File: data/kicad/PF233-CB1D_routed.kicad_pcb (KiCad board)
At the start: 6 copper layers, 78 x 77.2 mm, 70 parts, among them M5 5 V 1.5 A switching module, U1 Pico 2 W

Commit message: WIP: per-board 0.125 mm routing grid for AU1 / CB1D (0.5 mm-pitch rows on grid lines); fine zone radius in mm; AU1 route on the new grid running
Co-Authored-By: Claude Opus 5.5 <noreply@anthropic.com>
Claude-Session: https://claude.ai/code/session_01FX4DWSYYjMCFGGA6gmha65
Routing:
- net GYR_SDA: track 11.2 -> 6.59 mm, vias 2 -> 1
- net UG_VIO: track 14.9 -> 18.9 mm
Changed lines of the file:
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@@
   (gr_line (start 107.600 136.500) (end 92.400 136.500) (stroke (width 0.1) (type default)) (layer "Edge.Cuts"))
   (gr_line (start 92.400 136.500) (end 92.400 138.252) (stroke (width 0.1) (type default)) (layer "Edge.Cuts"))
-  (segment (start 106.9500 68.7000) (end 106.9500 69.3000) (width 0.2) (layer "F.Cu") (net 15))
-  (segment (start 106.9500 69.3000) (end 107.0000 68.5875) (width 0.2) (layer "F.Cu") (net 15))
-  (segment (start 106.5000 68.4000) (end 106.5000 67.9500) (width 0.2) (layer "F.Cu") (net 15))
-  (segment (start 106.5000 67.9500) (end 106.3500 67.8000) (width 0.2) (layer "F.Cu") (net 15))
-  (segment (start 106.3500 67.8000) (end 105.7750 67.0000) (width 0.2) (layer "F.Cu") (net 15))
+  (segment (start 106.9500 68.7000) (end 106.9500 69.3000) (width 0.15) (layer "F.Cu") (net 15))
+  (segment (start 106.9500 69.3000) (end 107.0000 68.5875) (width 0.15) (layer "F.Cu") (net 15))
+  (segment (start 106.5000 68.4000) (end 106.5000 67.9500) (width 0.15) (layer "F.Cu") (net 15))
+  (segment (start 106.5000 67.9500) (end 106.3500 67.8000) (width 0.15) (layer "F.Cu") (net 15))
+  (segment (start 106.3500 67.8000) (end 105.7750 67.0000) (width 0.15) (layer "F.Cu") (net 15))
   (segment (start 108.8900 75.1100) (end 108.4500 74.4000) (width 0.2) (layer "F.Cu") (net 16))
   (segment (start 108.4500 74.4000) (end 108.4500 72.3000) (width 0.2) (layer "F.Cu") (net 16))
-  (segment (start 108.4500 72.3000) (end 106.9500 70.8000) (width 0.2) (layer "F.Cu") (net 16))
-  (segment (start 106.9500 70.8000) (end 106.9500 70.5000) (width 0.2) (layer "F.Cu") (net 16))
+  (segment (start 108.4500 72.3000) (end 107.1000 70.9500) (width 0.15) (layer "F.Cu") (net 16))
+  (segment (start 107.1000 70.9500) (end 107.1000 70.6500) (width 0.15) (layer "F.Cu") (net 16))
+  (segment (start 107.1000 70.6500) (end 106.9500 70.5000) (width 0.15) (layer "F.Cu") (net 16))
   (segment (start 108.4500 72.3000) (end 109.5000 72.3000) (width 0.2) (layer "F.Cu") (net 16))
   (segment (start 109.5000 72.3000) (end 110.4000 71.4000) (width 0.2) (layer "F.Cu") (net 16))
@@
   (segment (start 112.3250 69.5000) (end 111.9000 70.0500) (width 0.2) (layer "F.Cu") (net 17))
   (segment (start 111.9000 70.0500) (end 112.3250 69.5000) (width 0.2) (layer "F.Cu") (net 17))
-  (segment (start 111.9000 70.8000) (end 108.7500 70.8000) (width 0.2) (layer "In2.Cu") (net 17))
-  (segment (start 108.7500 70.8000) (end 107.7000 70.8000) (width 0.2) (layer "F.Cu") (net 17))
-  (segment (start 107.7000 70.8000) (end 107.5500 70.6500) (width 0.2) (layer "F.Cu") (net 17))
-  (segment (start 107.5500 70.6500) (end 107.5500 70.5000) (width 0.2) (layer "F.Cu") (net 17))
-  (segment (start 108.0000 70.2000) (end 108.0000 69.7500) (width 0.2) (layer "F.Cu") (net 50))
-  (segment (start 108.0000 69.7500) (end 108.0000 69.3000) (width 0.2) (layer "F.Cu") (net 50))
-  (segment (start 108.0000 69.3000) (end 107.7000 69.3000) (width 0.2) (layer "F.Cu") (net 50))
-  (segment (start 107.7000 69.3000) (end 107.7000 69.1500) (width 0.2) (layer "F.Cu") (net 50))
-  (segment (start 107.7000 69.1500) (end 107.5500 69.1500) (width 0.2) (layer "F.Cu") (net 50))
-  (segment (start 107.5500 69.1500) (end 107.5500 68.7000) (width 0.2) (layer "F.Cu") (net 50))
-  (segment (start 107.5500 68.7000) (end 107.5500 67.6500) (width 0.2) (layer "F.Cu") (net 50))
-  (segment (start 107.5500 67.6500) (end 107.2250 67.0000) (width 0.2) (layer "F.Cu") (net 50))
-  (segment (start 107.2250 67.0000) (end 107.5500 67.6500) (width 0.2) (layer "F.Cu") (net 50))
-  (segment (start 107.5500 67.6500) (end 107.5500 66.9000) (width 0.2) (layer "F.Cu") (net 50))
-  (segment (start 107.5500 66.9000) (end 106.6500 66.0000) (width 0.2) (layer "F.Cu") (net 50))
+  (segment (start 108.0000 70.2000) (end 108.0000 69.7500) (width 0.15) (layer "F.Cu") (net 50))
+  (segment (start 108.0000 69.7500) (end 108.0000 69.3000) (width 0.15) (layer "F.Cu") (net 50))
+  (segment (start 108.0000 69.3000) (end 107.8500 69.3000) (width 0.15) (layer "F.Cu") (net 50))
+  (segment (start 107.8500 69.3000) (end 107.7000 69.1500) (width 0.15) (layer "F.Cu") (net 50))
+  (segment (start 107.7000 69.1500) (end 107.5500 69.1500) (width 0.15) (layer "F.Cu") (net 50))
+  (segment (start 107.5500 69.1500) (end 107.5500 68.7000) (width 0.15) (layer "F.Cu") (net 50))
+  (segment (start 107.5500 68.7000) (end 107.5500 67.6500) (width 0.15) (layer "F.Cu") (net 50))
+  (segment (start 107.5500 67.6500) (end 107.2250 67.0000) (width 0.15) (layer "F.Cu") (net 50))
+  (segment (start 107.2250 67.0000) (end 107.5500 67.6500) (width 0.15) (layer "F.Cu") (net 50))
+  (segment (start 107.5500 67.6500) (end 107.5500 66.9000) (width 0.15) (layer "F.Cu") (net 50))
+  (segment (start 107.5500 66.9000) (end 106.6500 66.0000) (width 0.15) (layer "F.Cu") (net 50))
   (segment (start 106.6500 66.0000) (end 106.5000 66.0000) (width 0.2) (layer "F.Cu") (net 50))
   (segment (start 106.5000 66.0000) (end 106.3500 65.8500) (width 0.2) (layer "F.Cu") (net 50))
@@
   (segment (start 104.7000 66.4500) (end 104.2250 67.0000) (width 0.2) (layer "F.Cu") (net 50))
   (segment (start 104.2250 67.0000) (end 104.7000 66.4500) (width 0.2) (layer "F.Cu") (net 50))
-  (segment (start 104.7000 66.4500) (end 104.7000 68.4000) (width 0.2) (layer "F.Cu") (net 50))
-  (segment (start 104.7000 68.4000) (end 104.2500 68.8500) (width 0.2) (layer "F.Cu") (net 50))
-  (segment (start 104.2500 68.8500) (end 103.8250 69.5000) (width 0.2) (layer "F.Cu") (net 50))
-  (segment (start 104.7000 68.4000) (end 105.4500 68.4000) (width 0.2) (layer "F.Cu") (net 50))
-  (segment (start 105.4500 68.4000) (end 105.7500 68.7000) (width 0.2) (layer "F.Cu") (net 50))
+  (segment (start 104.7000 66.4500) (end 104.7000 68.4000) (width 0.15) (layer "F.Cu") (net 50))
+  (segment (start 104.7000 68.4000) (end 104.2500 68.8500) (width 0.15) (layer "F.Cu") (net 50))
+  (segment (start 104.2500 68.8500) (end 103.8250 69.5000) (width 0.15) (layer "F.Cu") (net 50))
+  (segment (start 104.7000 68.4000) (end 105.4500 68.4000) (width 0.15) (layer "F.Cu") (net 50))
+  (segment (start 105.4500 68.4000) (end 105.7500 68.7000) (width 0.15) (layer "F.Cu") (net 50))
+  (segment (start 105.8375 68.7500) (end 105.6000 68.5500) (width 0.15) (layer "F.Cu") (net 50))
+  (segment (start 105.6000 68.5500) (end 105.3000 68.8500) (width 0.15) (layer "F.Cu") (net 50))
+  (segment (start 105.3000 68.8500) (end 105.3000 70.6500) (width 0.15) (layer "F.Cu") (net 50))
+  (segment (start 105.3000 70.6500) (end 106.3500 70.6500) (width 0.15) (layer "F.Cu") (net 50))
+  (segment (start 106.3500 70.6500) (end 106.3500 70.3500) (width 0.15) (layer "F.Cu") (net 50))
+  (segment (start 106.3500 70.3500) (end 106.5000 70.3500) (width 0.15) (layer "F.Cu") (net 50))
   (segment (start 88.9500 98.0000) (end 88.3500 98.7000) (width 0.2) (layer "F.Cu") (net 15))
   (segment (start 88.3500 98.7000) (end 88.3500 99.1500) (width 0.2) (layer "F.Cu") (net 15))
@@
   (segment (start 108.3000 66.4500) (end 108.3000 66.0000) (width 0.2) (layer "F.Cu") (net 15))
   (segment (start 108.3000 66.0000) (end 108.7750 67.0000) (width 0.2) (layer "F.Cu") (net 15))
-  (segment (start 105.7750 67.0000) (end 106.2000 67.6500) (width 0.2) (layer "F.Cu") (net 15))
-  (segment (start 106.2000 67.6500) (end 106.2000 68.1000) (width 0.2) (layer "F.Cu") (net 15))
-  (segment (start 106.2000 68.1000) (end 106.5000 68.5875) (width 0.2) (layer "F.Cu") (net 15))
+  (segment (start 105.7750 67.0000) (end 106.2000 67.6500) (width 0.15) (layer "F.Cu") (net 15))
+  (segment (start 106.2000 67.6500) (end 106.2000 68.1000) (width 0.15) (layer "F.Cu") (net 15))
+  (segment (start 106.2000 68.1000) (end 106.5000 68.5875) (width 0.15) (layer "F.Cu") (net 15))
   (segment (start 99.7000 95.5550) (end 98.8500 95.2500) (width 0.3) (layer "F.Cu") (net 31))
   (segment (start 98.8500 95.2500) (end 98.4000 95.2500) (width 0.3) (layer "F.Cu") (net 31))
@@
   (segment (start 126.6000 77.4000) (end 126.7250 78.0000) (width 0.2) (layer "F.Cu") (net 51))
   (segment (start 98.4000 120.9000) (end 98.8500 120.7500) (width 0.2) (layer "F.Cu") (net 15))
-  (segment (start 106.2000 68.1000) (end 106.3500 67.8000) (width 0.2) (layer "F.Cu") (net 15))
+  (segment (start 106.2000 68.1000) (end 106.3500 67.8000) (width 0.15) (layer "F.Cu") (net 15))
   (segment (start 111.0000 73.0500) (end 110.8500 73.0500) (width 0.2) (layer "F.Cu") (net 11))
   (segment (start 111.0000 73.0500) (end 110.8500 73.0500) (width 0.2) (layer "In3.Cu") (net 11))
@@
   (via (at 106.3500 67.8000) (size 0.6) (drill 0.3) (layers "F.Cu" "B.Cu") (net 15))
   (via (at 111.9000 70.0500) (size 0.6) (drill 0.3) (layers "F.Cu" "B.Cu") (net 17))
-  (via (at 108.7500 70.8000) (size 0.6) (drill 0.3) (layers "F.Cu" "B.Cu") (net 17))
   (via (at 88.3500 99.1500) (size 0.6) (drill 0.3) (layers "F.Cu" "B.Cu") (net 15))
   (via (at 86.8500 94.5000) (size 0.6) (drill 0.3) (layers "F.Cu" "B.Cu") (net 15))

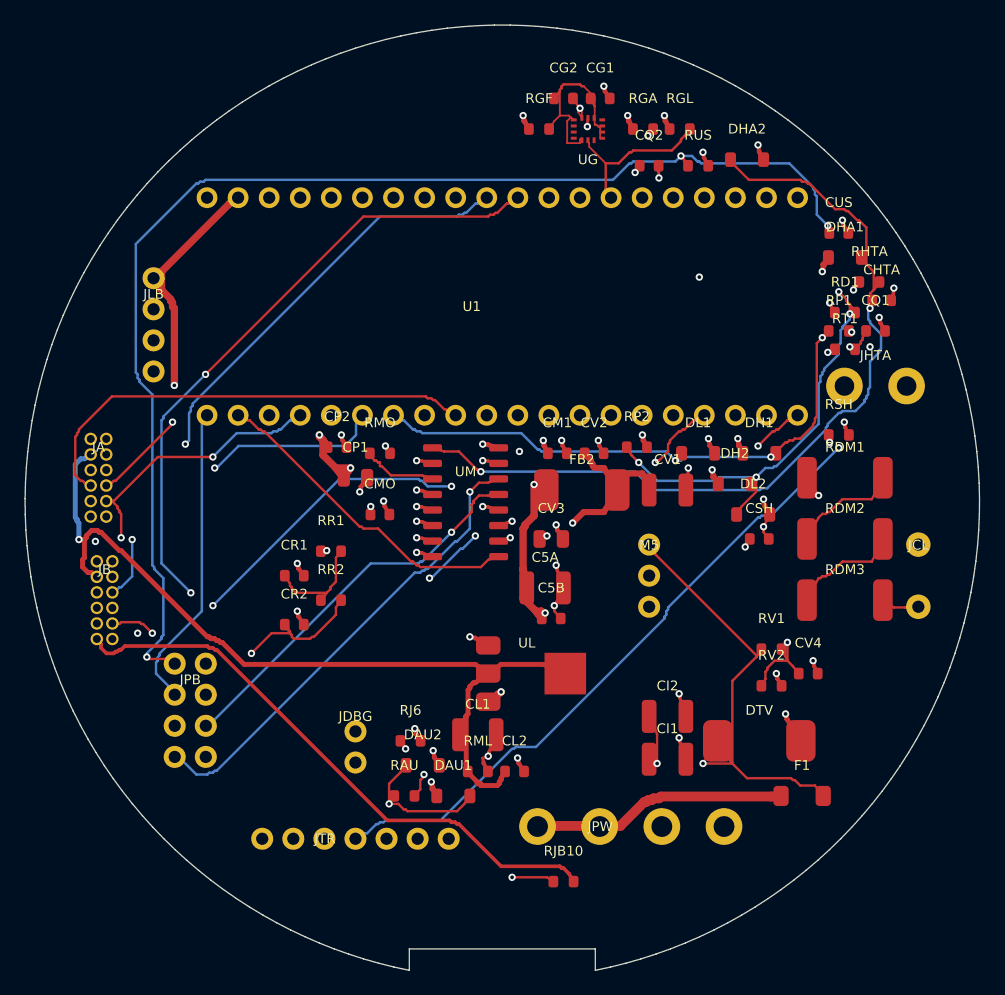
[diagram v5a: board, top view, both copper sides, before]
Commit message: WIP (NOT signed off): sign-off outputs with AU1 38 / 38 (exact DRC 0 / 0, all AU1 checks pass); CB1D 45 / 46 (TRIG_EXT open on the 0.125 grid, being re-routed on 0.15)
Co-Authored-By: Claude Opus 5.5 <noreply@anthropic.com>
Claude-Session: https://claude.ai/code/session_01FX4DWSYYjMCFGGA6gmha65
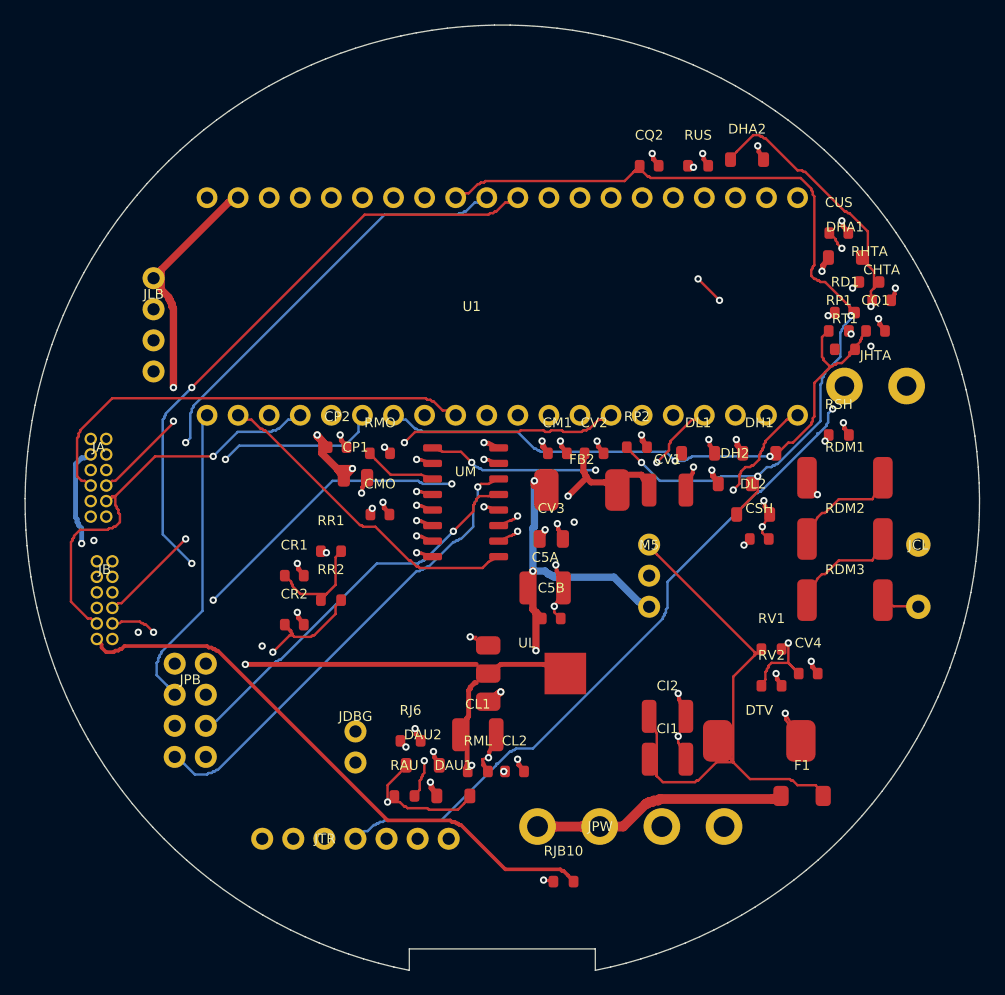
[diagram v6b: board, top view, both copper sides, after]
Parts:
- removed CG1, CG2: 100n, Capacitor_SMD:C_0603_1608Metric
- removed RGA, RGL: 4k7, Resistor_SMD:R_0603_1608Metric
- removed RGF: 10R, Resistor_SMD:R_0603_1608Metric
- removed UG: BMI270, PF233:BMI270_LGA-14_2.5x3.0mm
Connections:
- U1 pad 26: GYR_SDA -> (no net)
- U1 pad 27: GYR_SCL -> (no net)
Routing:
- net TRIG_EXT: track 64.4 -> 0.00 mm, vias 1 -> 0
- net UG_VIO: track 18.9 -> 0.00 mm
- net GYR_SCL: track 13.5 -> 0.00 mm
- net GND: track 117.3 -> 109.0 mm, vias 42 -> 39
- net P3V3: track 26.7 -> 19.4 mm, vias 12 -> 9
- net GYR_SDA: track 6.59 -> 0.00 mm, vias 1 -> 0
- net DIAL_EXT: track 71.0 -> 65.2 mm
- net UMB_SHLD: track 103.9 -> 99.8 mm
- net BLANK: track 38.0 -> 34.3 mm, vias 2 -> 1
- net +5V: track 96.5 -> 98.7 mm, vias 6 -> 7
- net AUD_PIO: track 46.1 -> 47.6 mm
- net MUX_S0: track 52.7 -> 51.2 mm
- net MUX_S1: track 54.1 -> 52.7 mm
- net +3V3D: track 75.0 -> 73.7 mm, vias 1 -> 4
- net JB10_VCM: track 44.8 -> 46.0 mm
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
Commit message: WIP: sign-off outputs (73 PASS / 1 FAIL before the HV count fix; rerun in progress)
Co-Authored-By: Claude Opus 5.5 <noreply@anthropic.com>
Claude-Session: https://claude.ai/code/session_01FX4DWSYYjMCFGGA6gmha65
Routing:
- net TRIG_EXT: track 0.00 -> 64.4 mm, vias 0 -> 1
- net DIAL_EXT: track 65.2 -> 71.0 mm
- net BLANK: track 34.3 -> 38.0 mm, vias 1 -> 2
- net UMB_SHLD: track 99.8 -> 102.1 mm
- net +5V: track 98.7 -> 96.5 mm, vias 7 -> 6
- net HTA_IN: track 72.6 -> 74.3 mm, vias 3 -> 2
- net AUD_PIO: track 47.6 -> 46.1 mm
- net MUX_S0: track 51.2 -> 52.7 mm
- net DIAL_IN: track 80.4 -> 78.9 mm
- net GND: track 109.0 -> 110.3 mm
- net MUX_S1: track 52.7 -> 54.1 mm
- net +3V3D: track 73.7 -> 75.0 mm, vias 4 -> 1
- net JB10_VCM: track 46.0 -> 44.8 mm
- net VBUS_SENSE: track 73.4 -> 72.7 mm, vias 3 -> 2
- net SCLK: track 38.1 -> 38.8 mm
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
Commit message: Close-out of the output modes / audio / gyro integration: sign-off 76 PASS / 0 FAIL / 4 UNVERIFIED, strict regress 114 / 0, release controls 12 / 12, publish 0 stale
AU1 (36 x 60, 8 layers, gyro moved from CB1D) routed 38 / 38, CB1D-C2 46 / 46, both exact DRC 0 / 0; PB1R-v5 AWG12 solder holes; PM2-B, HB2-B; superseded Gerber sets marked.
Tooling now default: exact-geometry DRC, router fine-pitch keep-out / neck-down / per-board grid, local repair, round checkpoints, non-destructive reset,
interface check, AU1 3-D models with gull-wing leads, counted HV check; pad check traced by the pipeline; process-guard regress row; PROCESS.md / CLAUDE.md / handoff updated.

Co-Authored-By: Claude Opus 5.5 <noreply@anthropic.com>
Claude-Session: https://claude.ai/code/session_01FX4DWSYYjMCFGGA6gmha65
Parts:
- removed the JCL at (134.0, 106.0)
- removed the JDBG at (88.0, 120.0)
- removed the JPB at (74.5, 117.0)
- removed the JPW at (110.5, 126.5)
- removed the JTR at (88.0, 127.5)
- added JCL: Coil taps from TXJ1: COIL_B (drain side), COIL_A (VBUS side), Connector:Wire_pads_AWG22_1x2_P5.08mm, F.Cu at (134.0, 106.0)
- added JDBG: RUN / GND (reset, SWD pads on Pico underside), Connector:Wire_pads_1x2_P2.54mm, F.Cu at (88.0, 120.0)
- added JPB: to PB1R: 12V GND TX1_IN REF_I1 FAULT1_N ISENSE1 NTC GND, Connector:Wire_pads_2x4_P2.54mm, F.Cu at (74.5, 117.0)
- added JPW: Power in: VBUS VBUS GND GND (from shaft), Connector:Wire_pads_1x4_P5.08mm, F.Cu at (110.5, 126.5)
- added JTR: Handle: +3V3 GND TRIG DIAL AUD_LINK - SHLD, Connector:Wire_pads_1x7_P2.54mm, F.Cu at (88.0, 127.5)
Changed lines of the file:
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@@
     (pad "40" thru_hole circle (at 8.890 -24.130 90) (size 1.7 1.7) (drill 1.0) (layers "*.Cu" "*.Mask") (net 0 ""))
   )
-  (footprint "Connector:Pin_header_1x2_P2.54mm" (layer "F.Cu") (at 88.0000 120.0000)
+  (footprint "Connector:Wire_pads_1x2_P2.54mm" (layer "F.Cu") (at 88.0000 120.0000)
     (property "Reference" "JDBG" (at 0 -2.5 0) (layer "F.SilkS") (effects (font (size 0.8 0.8) (thickness 0.12))))
     (property "Value" "RUN / GND (reset, SWD pads on Pico underside)" (at 0 2.5 0) (layer "F.Fab") (effects (font (size 0.8 0.8) (thickness 0.12))))
@@
     (pad "2" smd roundrect (at 0.775 0.000) (size 0.800 0.950) (layers "F.Cu" "F.Paste" "F.Mask") (net 15 "GND"))
   )
-  (footprint "Connector:Terminal_block_1x4_P5.08mm" (layer "F.Cu") (at 110.5000 126.5000 90)
+  (footprint "Connector:Wire_pads_1x4_P5.08mm" (layer "F.Cu") (at 110.5000 126.5000 90)
     (property "Reference" "JPW" (at 0 -2.5 0) (layer "F.SilkS") (effects (font (size 0.8 0.8) (thickness 0.12))))
     (property "Value" "Power in: VBUS VBUS GND GND (from shaft)" (at 0 2.5 0) (layer "F.Fab") (effects (font (size 0.8 0.8) (thickness 0.12))))
@@
     (pad "2" smd roundrect (at 0.775 0.000) (size 0.800 0.950) (layers "F.Cu" "F.Paste" "F.Mask") (net 15 "GND"))
   )
-  (footprint "Connector:Pin_header_1x7_P2.54mm" (layer "F.Cu") (at 88.0000 127.5000 90)
+  (footprint "Connector:Wire_pads_1x7_P2.54mm" (layer "F.Cu") (at 88.0000 127.5000 90)
     (property "Reference" "JTR" (at 0 -2.5 0) (layer "F.SilkS") (effects (font (size 0.8 0.8) (thickness 0.12))))
     (property "Value" "Handle: +3V3 GND TRIG DIAL AUD_LINK - SHLD" (at 0 2.5 0) (layer "F.Fab") (effects (font (size 0.8 0.8) (thickness 0.12))))
@@
     (pad "12" thru_hole circle (at 0.635 3.175) (size 1.02 1.02) (drill 0.65) (layers "*.Cu" "*.Mask") (net 15 "GND"))
   )
-  (footprint "Connector:Pin_header_2x4_P2.54mm" (layer "F.Cu") (at 74.5000 117.0000)
+  (footprint "Connector:Wire_pads_2x4_P2.54mm" (layer "F.Cu") (at 74.5000 117.0000)
     (property "Reference" "JPB" (at 0 -2.5 0) (layer "F.SilkS") (effects (font (size 0.8 0.8) (thickness 0.12))))
     (property "Value" "to PB1R: 12V GND TX1_IN REF_I1 FAULT1_N ISENSE1 NTC GND" (at 0 2.5 0) (layer "F.Fab") (effects (font (size 0.8 0.8) (thickness 0.12))))
@@
     (pad "2" smd roundrect (at 0.775 0.000) (size 0.800 0.950) (layers "F.Cu" "F.Paste" "F.Mask") (net 15 "GND"))
   )
-  (footprint "Connector:Solder_holes_AWG22_1x2_P5.08mm" (layer "F.Cu") (at 134.0000 106.0000)
+  (footprint "Connector:Wire_pads_AWG22_1x2_P5.08mm" (layer "F.Cu") (at 134.0000 106.0000)
     (property "Reference" "JCL" (at 0 -2.5 0) (layer "F.SilkS") (effects (font (size 0.8 0.8) (thickness 0.12))))
     (property "Value" "Coil taps from TXJ1: COIL_B (drain side), COIL_A (VBUS side)" (at 0 2.5 0) (layer "F.Fab") (effects (font (size 0.8 0.8) (thickness 0.12))))
